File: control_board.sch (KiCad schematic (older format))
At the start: 44 parts, among them J1 Servo_1_Conn, J10 LED_2_Conn, J11 LED_3_Conn, J12 LED_4_Conn, J13 Raspberry_Pi_Conn, J14 DC_Power_Header, J15 USB_Power_Jumper, J16 Jack-DC, J17 Herkulex Conn, J2 Servo_2_Conn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

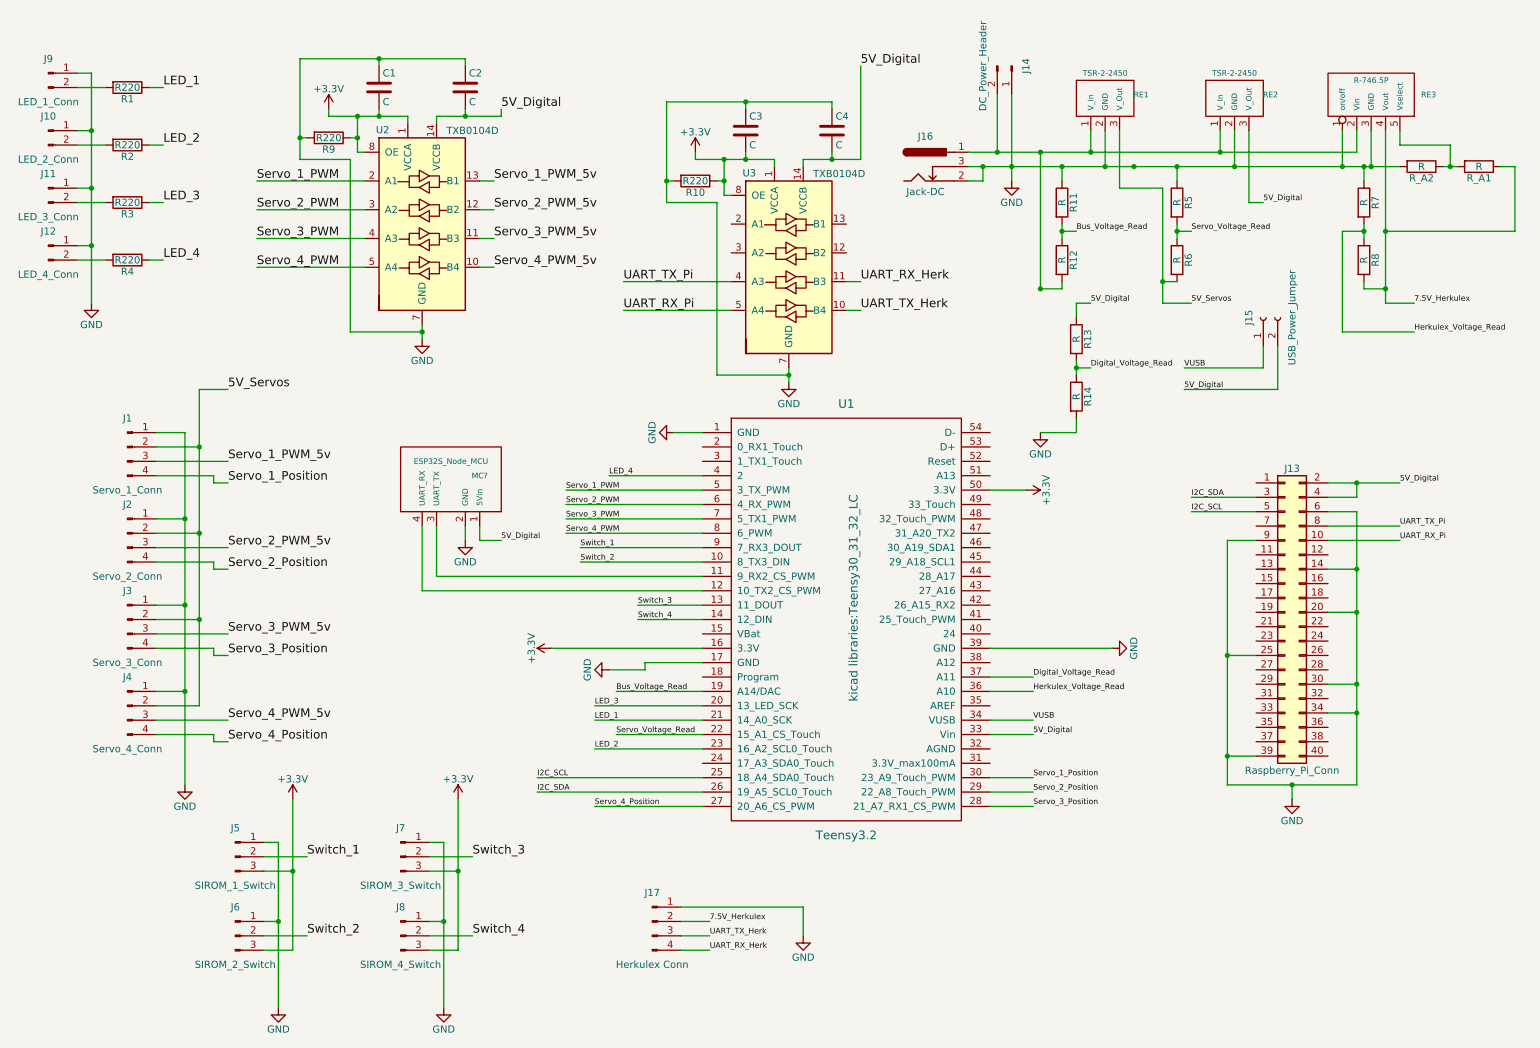
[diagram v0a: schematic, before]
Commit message: Added resistor values, correct 7.5V reg enable pin and output cap
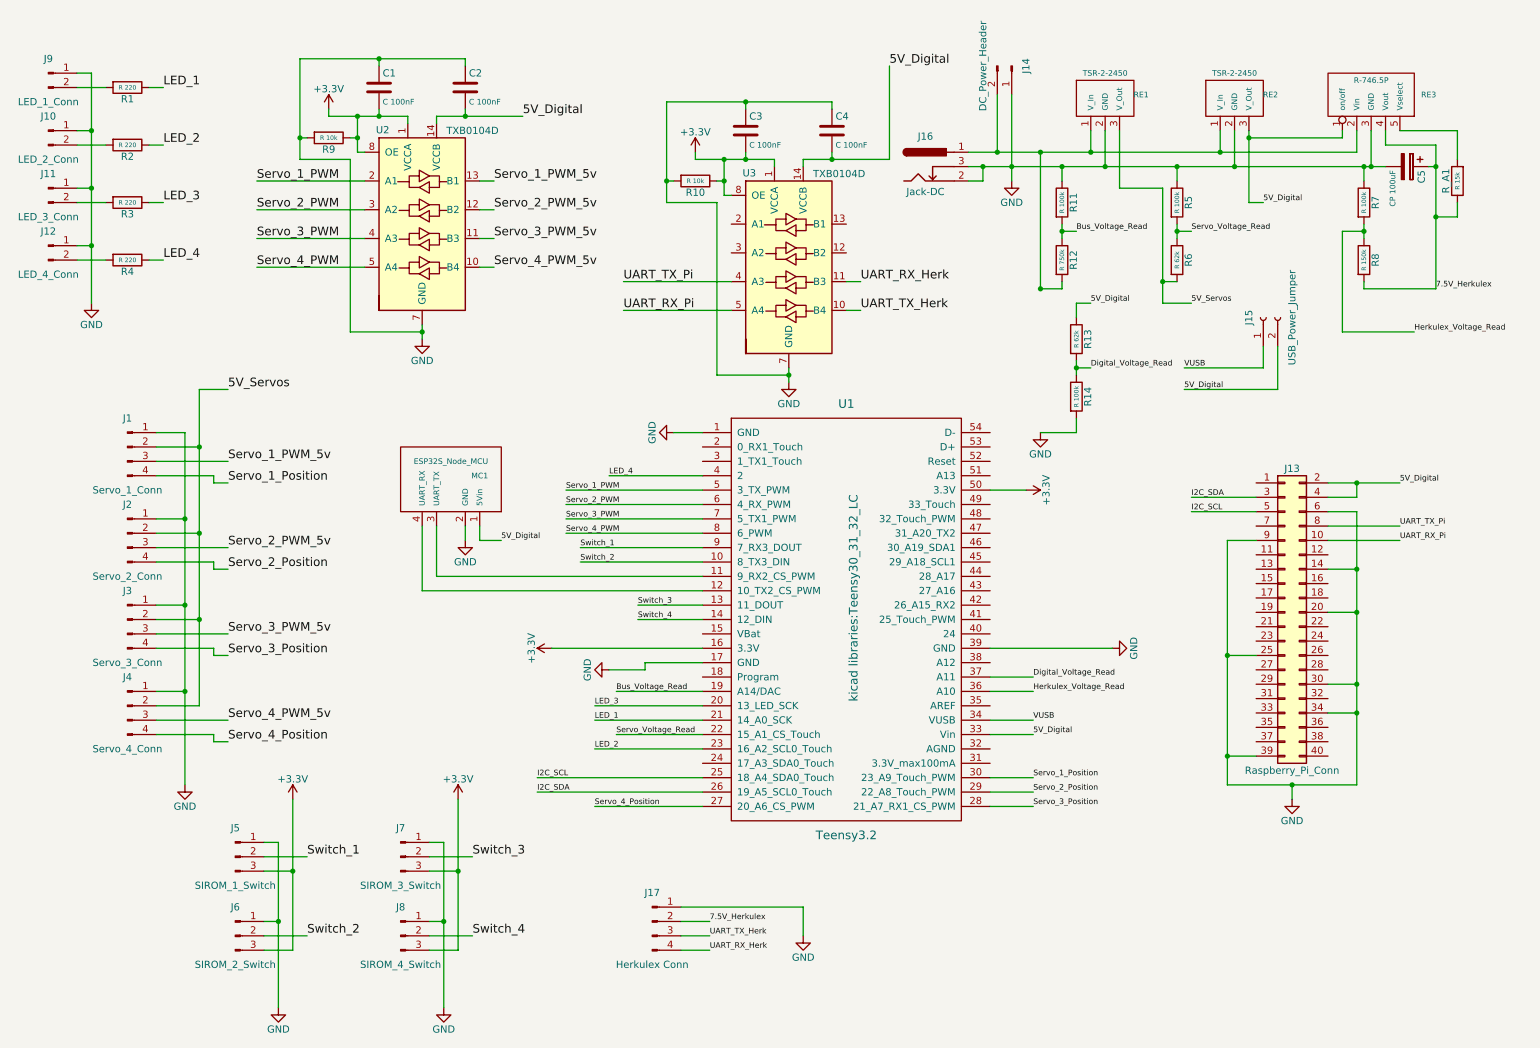
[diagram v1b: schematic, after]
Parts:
- removed R_A2: R, Resistors_SMD:R_1206_HandSoldering, symbol R
- added C5: CP 100uF, Capacitors_THT:CP_Radial_D5.0mm_P2.50mm, symbol CP
- C1, C2, C3, C4: value C -> C 100nF
- R1, R2, R3, R4: value R220 -> R 220
- R10, R9: value R220 -> R 10k
- R11, R14, R5, R7: value R -> R 100k
- R12: value R -> R 750k
- R13, R6: value R -> R 62k
- R8: value R -> R 150k
- R_A1: value R -> R 15k
- gave numbers to parts that had none: 1
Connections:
- net 5V_Digital: now also RE3.1 (on/off)
- net 7.5V_Herkulex: now also C5.1
- net GND: now also C5.2; no longer RE3.1 (on/off)
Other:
- moved on the sheet: R_A1
